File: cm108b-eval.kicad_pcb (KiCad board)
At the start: 2 copper layers, 16 x 35 mm, 3 parts, among them IC1 CM108B, J1 USB_A

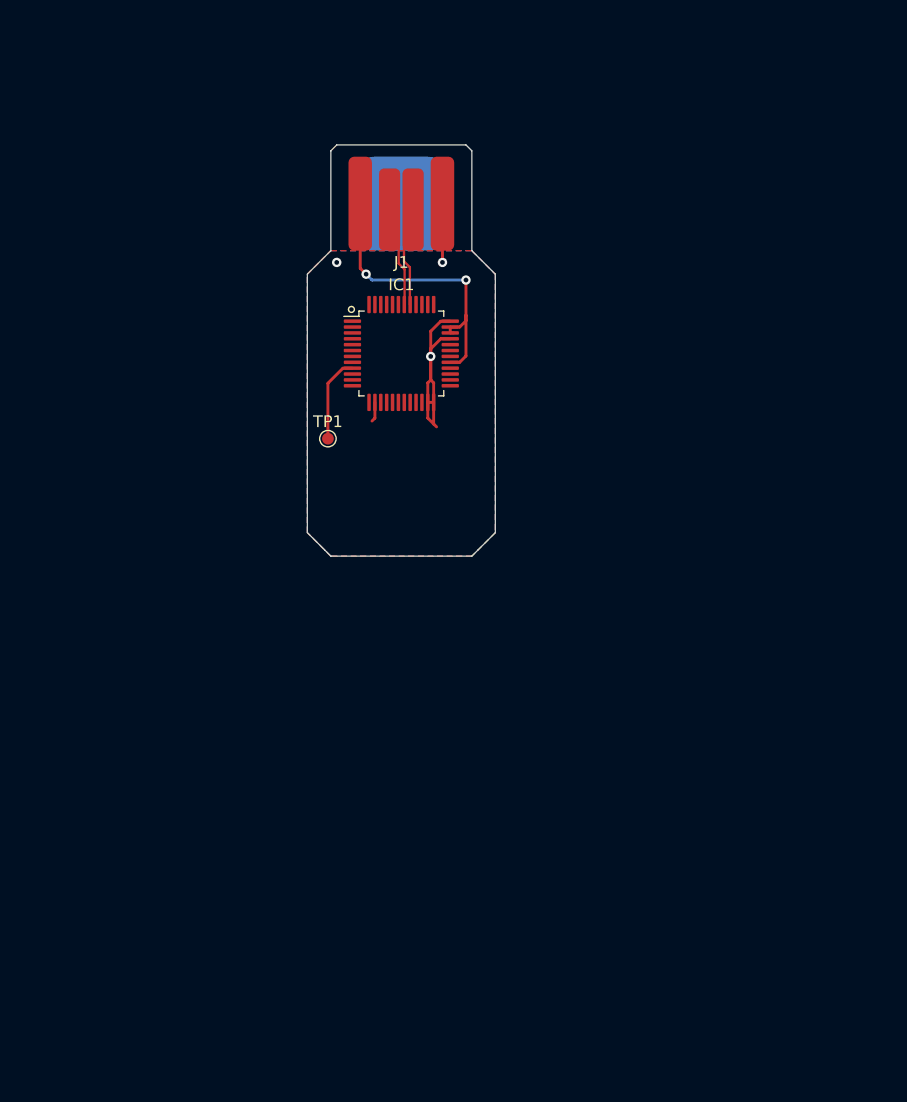
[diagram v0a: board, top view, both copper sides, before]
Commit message: Footprints assigned
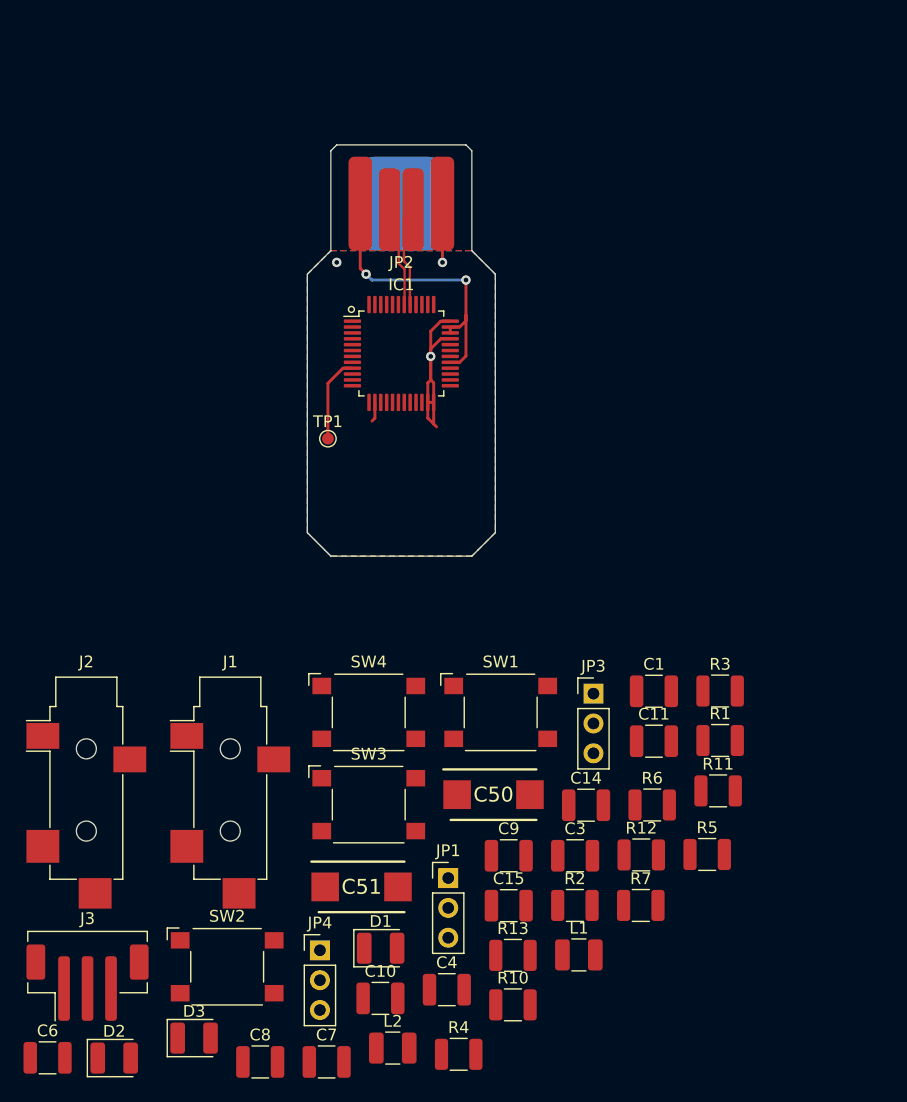
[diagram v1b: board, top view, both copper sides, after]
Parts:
- added C1: 10uF, Capacitor_SMD:C_1210_3225Metric, F.Cu at (170.5, 126.5)
- added C10: 104, Capacitor_SMD:C_1210_3225Metric, F.Cu at (147.2, 152.6)
- added C11: 105, Capacitor_SMD:C_1210_3225Metric, F.Cu at (170.5, 130.8)
- added C14: 475, Capacitor_SMD:C_1210_3225Metric, F.Cu at (164.7, 136.2)
- added C15: 475, Capacitor_SMD:C_1210_3225Metric, F.Cu at (158.1, 144.8)
- added C3: 101, Capacitor_SMD:C_1210_3225Metric, F.Cu at (163.8, 140.5)
- added C4: 101, Capacitor_SMD:C_1210_3225Metric, F.Cu at (152.9, 151.9)
- added C50: 470uF, 293D477X9010E2TE3:CAPPM7343X430N, F.Cu at (156.8, 135.3)
- added C51: 470uF, 293D477X9010E2TE3:CAPPM7343X430N, F.Cu at (145.6, 143.2)
- added C6: 104, Capacitor_SMD:C_1210_3225Metric, F.Cu at (118.9, 157.7)
- added C7: 475, Capacitor_SMD:C_1210_3225Metric, F.Cu at (142.6, 158.1)
- added C8: 104, Capacitor_SMD:C_1210_3225Metric, F.Cu at (137.0, 158.1)
- added C9: 475, Capacitor_SMD:C_1210_3225Metric, F.Cu at (158.1, 140.5)
- added D1: OPER, LED_SMD:LED_1210_3225Metric, F.Cu at (147.2, 148.4)
- added D2: REC_MUTE, LED_SMD:LED_1210_3225Metric, F.Cu at (124.6, 157.7)
- added D3: POWER_DOWN, LED_SMD:LED_1210_3225Metric, F.Cu at (131.4, 156.0)
- added J1: SPRK, Connector_Audio:Jack_3.5mm_CUI_SJ-3524-SMT_Horizontal, F.Cu at (134.4, 133.9)
- added J2: MIC, Connector_Audio:Jack_3.5mm_CUI_SJ-3524-SMT_Horizontal, F.Cu at (122.2, 133.9)
- added J3: RADIO_DATA, Connector_JST:JST_PH_B3B-PH-SM4-TB_1x03-1MP_P2.00mm_Vertical, F.Cu at (122.3, 151.3)
- added JP1: PWRSEL, Connector_PinHeader_2.54mm:PinHeader_1x03_P2.54mm_Vertical, F.Cu at (153.0, 142.4)
- added JP3: MODE, Connector_PinHeader_2.54mm:PinHeader_1x03_P2.54mm_Vertical, F.Cu at (165.3, 126.7)
- added JP4: MSEL, Connector_PinHeader_2.54mm:PinHeader_1x03_P2.54mm_Vertical, F.Cu at (142.1, 148.6)
- added L1: L, Inductor_SMD:L_1210_3225Metric, F.Cu at (164.1, 148.9)
- added L2: L, Inductor_SMD:L_1210_3225Metric, F.Cu at (148.3, 156.9)
- added R1: 22Ω, Resistor_SMD:R_1210_3225Metric, F.Cu at (176.1, 130.7)
- added R10: 2.2kΩ, Resistor_SMD:R_1210_3225Metric, F.Cu at (158.5, 153.2)
- added R11: 330, Resistor_SMD:R_1210_3225Metric, F.Cu at (176.0, 135.0)
- added R12: 330, Resistor_SMD:R_1210_3225Metric, F.Cu at (169.4, 140.4)
- added R13: 1.2kΩ, Resistor_SMD:R_1210_3225Metric, F.Cu at (158.5, 149.0)
- added R2: 22Ω, Resistor_SMD:R_1210_3225Metric, F.Cu at (163.8, 144.7)
- added R3: 0Ω, Resistor_SMD:R_1210_3225Metric, F.Cu at (176.1, 126.5)
- added R4: 0Ω, Resistor_SMD:R_1210_3225Metric, F.Cu at (153.9, 157.4)
- added R5: 0Ω, Resistor_SMD:R_1210_3225Metric, F.Cu at (175.0, 140.4)
- added R6: 0Ω, Resistor_SMD:R_1210_3225Metric, F.Cu at (170.3, 136.2)
- added R7: 330, Resistor_SMD:R_1210_3225Metric, F.Cu at (169.4, 144.7)
- added SW1: MUTE_REC, Button_Switch_SMD:SW_SPST_Omron_B3FS-100xP, F.Cu at (157.5, 128.3)
- added SW2: MUTE_PLAY, Button_Switch_SMD:SW_SPST_Omron_B3FS-100xP, F.Cu at (134.2, 149.9)
- added SW3: VOL_DN, Button_Switch_SMD:SW_SPST_Omron_B3FS-100xP, F.Cu at (146.2, 136.2)
- added SW4: VOL_UP, Button_Switch_SMD:SW_SPST_Omron_B3FS-100xP, F.Cu at (146.2, 128.3)
- renumbered J1 to JP2
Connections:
- IC1 pad 10: (no net) -> /MODE
- IC1 pad 12: (no net) -> /LEDO
- IC1 pad 16: (no net) -> GND
- IC1 pad 18: (no net) -> /MUTEP
- IC1 pad 21: (no net) -> /LEDR
- IC1 pad 22: (no net) -> GND
- IC1 pad 25: (no net) -> Net-(IC1-Pad25)
- IC1 pad 26: (no net) -> Net-(C14-Pad2)
- IC1 pad 27: (no net) -> Net-(C11-Pad2)
- IC1 pad 29: VBUS -> Net-(C6-Pad1)
- IC1 pad 30: (no net) -> Net-(C51-Pad1)
- IC1 pad 32: (no net) -> Net-(C50-Pad1)
- IC1 pad 34: VBUS -> Net-(C8-Pad1)
- IC1 pad 38: (no net) -> /MSEL
- IC1 pad 39: (no net) -> /VOLUP
- IC1 pad 40: (no net) -> /PDSW
- IC1 pad 48: (no net) -> /VOLDN
- IC1 pad 6: (no net) -> /MUTER
- IC1 pad 7: (no net) -> /PWRSEL
- JP2 pad 1: VBUS -> Net-(JP2-Pad1)
- JP2 pad 2: /D- -> Net-(C3-Pad1)
- JP2 pad 3: /D+ -> Net-(C4-Pad1)
- JP2 pad 4: GND -> Net-(JP2-Pad4)
- JP2 pad 5: (no net) -> GND
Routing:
- net Net-(JP2-Pad4): track 0.00 -> 5.00 mm, vias 0 -> 1
- net GND: track 26.3 -> 21.3 mm, vias 3 -> 2

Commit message: PCB laid out
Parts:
- C11: value 105 -> 1uF
- C14, C15, C7, C9: value 475 -> 4.7uF
- C3, C4: value 101 -> 100pF
- C6, C8: value 104 -> 100nF
- D3: value POWER_DOWN -> PWR_DN
- JP2: footprint usb-a-edge:USB-A_trace -> Connector_USB:USB_Micro-B_Molex_47346-0001
- moved L2 82.9 mm to (150.0, 74.0), turned to 180 degrees
- moved SW2 81.3 mm to (183.0, 85.0)
- moved C6 78.7 mm to (169.0, 97.0), turned to 270 degrees
- moved C8 75.2 mm to (169.0, 90.0), turned to 90 degrees
- moved L1 75.2 mm to (170.0, 74.0)
- moved JP4 74.6 mm to (144.0, 74.0)
- moved C10 74.4 mm to (173.5, 83.0), turned to 180 degrees
- moved JP1 71.0 mm to (134.0, 74.0)
- moved C4 70.9 mm to (154.0, 81.0), turned to 270 degrees
- moved C7 68.2 mm to (173.0, 97.0), turned to 270 degrees
- moved R4 66.7 mm to (177.5, 95.0)
- moved R2 64.0 mm to (158.0, 81.0), turned to 90 degrees
- moved J3 62.4 mm to (135.8, 90.4), turned to 90 degrees
- moved C3 59.6 mm to (167.0, 81.0), turned to 270 degrees
- moved SW1 59.1 mm to (183.0, 75.0)
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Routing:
- net /VOLDN: track 0.00 -> 64.6 mm, vias 0 -> 2
- net +3V3: track 7.34 -> 70.2 mm, vias 0 -> 2
- net /AUDIO_R: track 0.00 -> 40.6 mm, vias 0 -> 2
- net /MUTER: track 0.00 -> 36.6 mm, vias 0 -> 2
- net /VOLUP: track 0.00 -> 34.8 mm, vias 0 -> 4
- net /MIC_IN: track 0.00 -> 34.6 mm, vias 0 -> 2
- net /AUDIO_L: track 0.00 -> 32.8 mm
- net /PWRSEL: track 0.00 -> 30.8 mm, vias 0 -> 2
- net /MUTEP: track 0.00 -> 30.1 mm, vias 0 -> 2
- net /PDSW: track 0.00 -> 29.9 mm, vias 0 -> 2
- net /MODE: track 0.00 -> 29.8 mm
- net Net-(C14-Pad2): track 0.00 -> 25.0 mm
- net /MSEL: track 0.00 -> 24.3 mm
- net /MIC_BIAS: track 0.00 -> 23.0 mm
- net Net-(C15-Pad2): track 0.00 -> 19.9 mm
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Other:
- board size 16 x 35 mm -> 60 x 50 mm
- board text added: "CM108B Audio Evaluation Board v1 C. Keller 2021-03-22"
- board text added: "CM108B USB Audio"

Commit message: Completed BOM
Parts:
- C1: value 10uF -> 10μF
- C10: value 104 -> 100nF
- C11: value 1uF -> 1μF
- C14, C15, C7, C9: value 4.7uF -> 4.7μF
- C50, C51: value 470uF -> 470μF
- D1, D2, D3: footprint LED_SMD:LED_1210_3225Metric -> LED_SMD:LED_0603_1608Metric
- J1: value SPRK -> SPKR
- R11, R12, R7: value 330 -> 330Ω
- moved TP1 0.50 mm to (142.5, 117.5)
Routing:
- net Net-(D3-Pad2): track 3.54 -> 4.65 mm
- net Net-(D2-Pad2): track 3.54 -> 4.15 mm
- net Net-(D1-Pad2): track 3.54 -> 4.15 mm
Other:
- board text added: "+"
- board text added: "CM108B Audio Evaluation Board v2 C. Keller 2021-03-23"
- board text removed: "CM108B Audio Evaluation Board v1 C. Keller 2021-03-22"

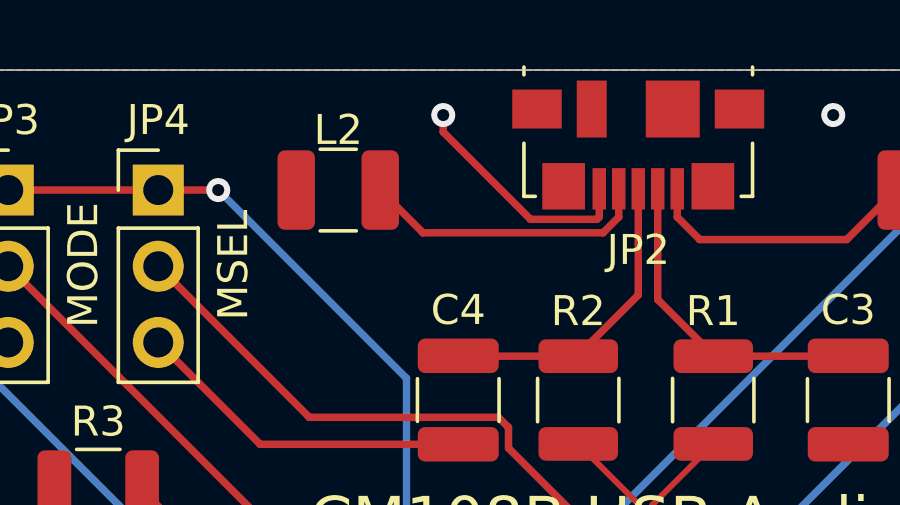
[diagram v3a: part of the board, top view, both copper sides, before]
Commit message: Move inductor to USB cable shield
Having it on the cable's ground pin just doesn't make sense to me.
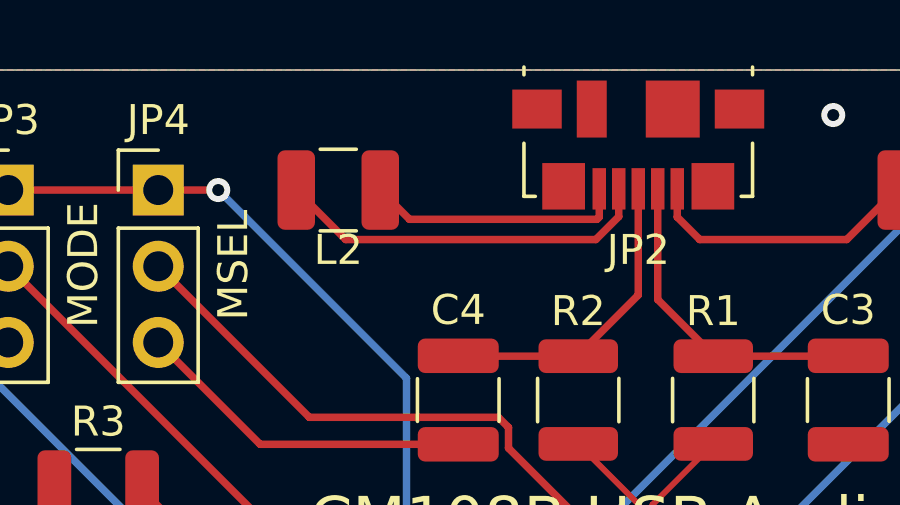
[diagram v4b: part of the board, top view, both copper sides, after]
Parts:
- turned L2 to 0 degrees
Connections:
- JP2 pad 4: Net-(JP2-Pad4) -> GND
- JP2 pad 5: GND -> Net-(JP2-Pad5)
- L2 pad 1: Net-(JP2-Pad4) -> GND
- L2 pad 2: GND -> Net-(JP2-Pad5)
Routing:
- net Net-(JP2-Pad4): track 9.70 -> 0.00 mm
- net Net-(JP2-Pad5): track 0.00 -> 8.67 mm
- net GND: track 41.1 -> 45.9 mm, vias 17 -> 16

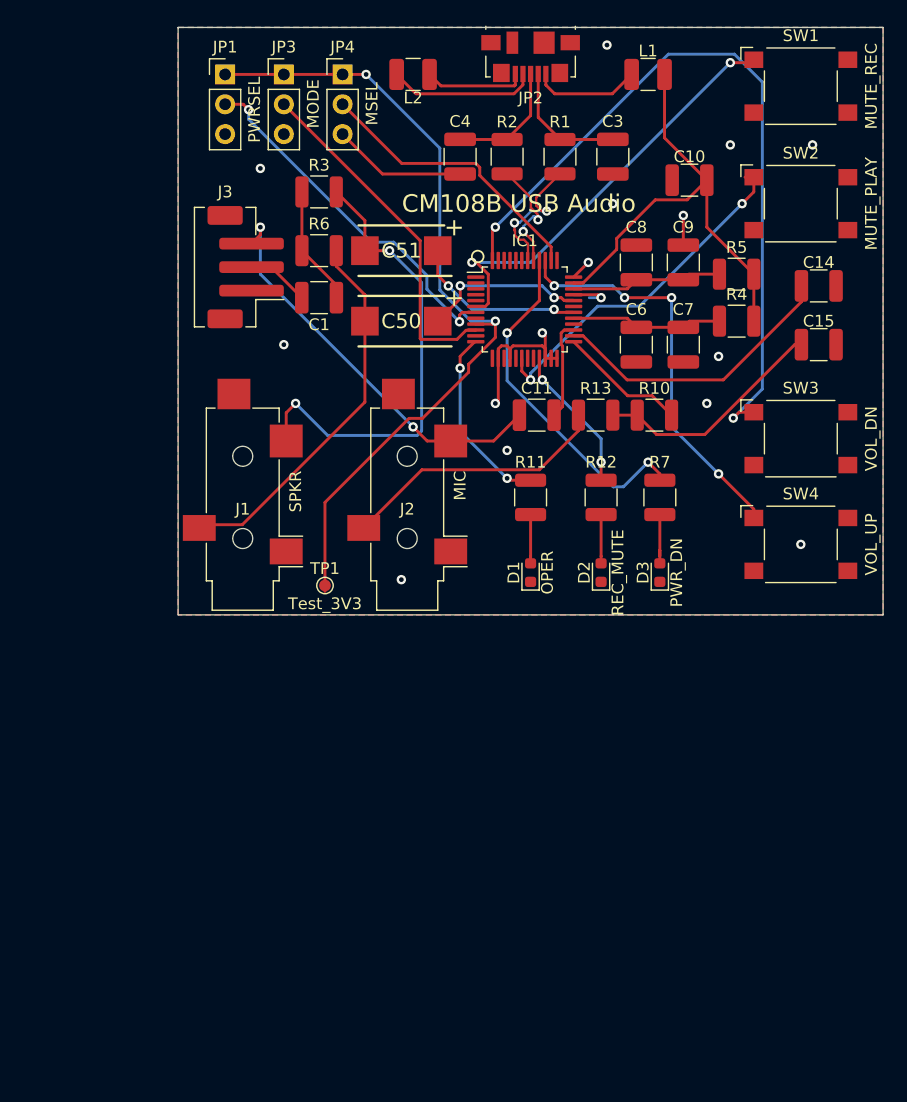
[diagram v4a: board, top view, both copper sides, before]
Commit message: Add some 3D models
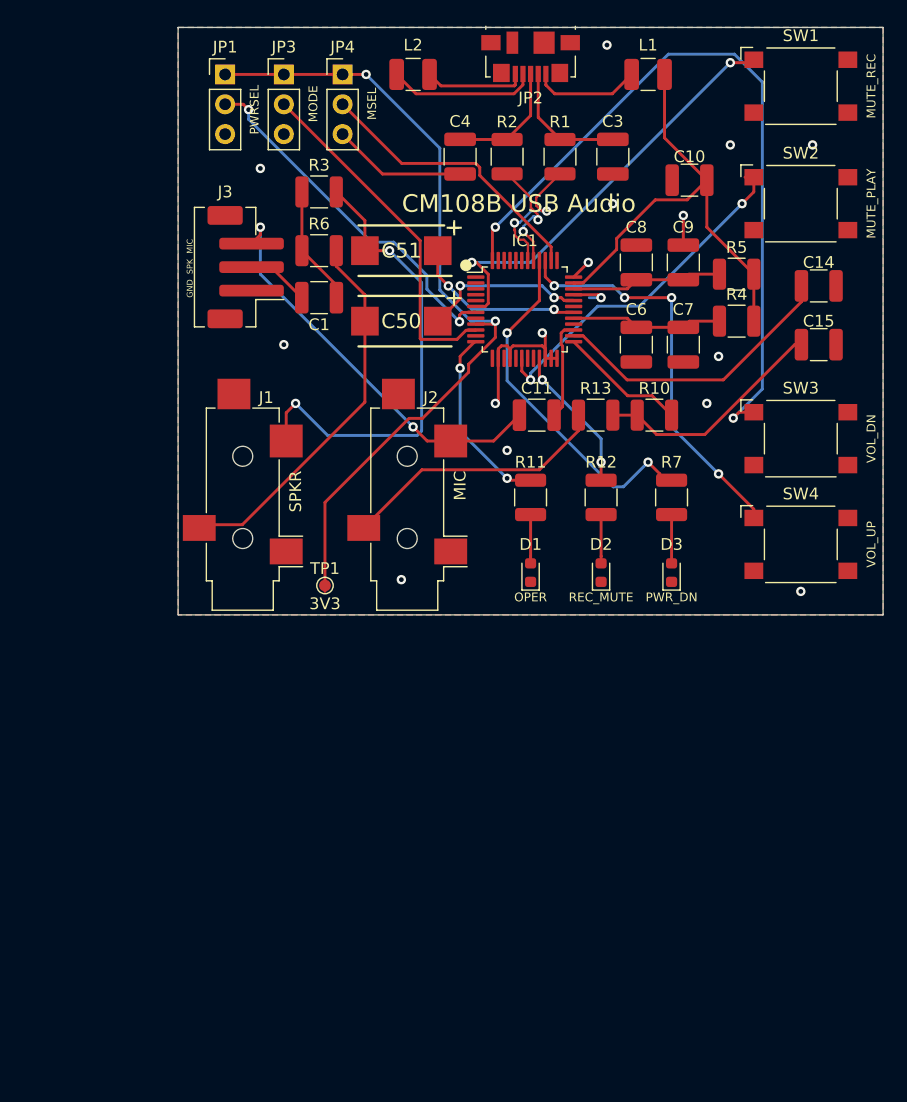
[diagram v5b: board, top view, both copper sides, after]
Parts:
- TP1: value Test_3V3 -> 3V3
- moved D3 1.00 mm to (172.0, 116.4)
- moved R7 1.00 mm to (172.0, 110.0)
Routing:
- net Net-(D3-Pad2): track 4.65 -> 4.15 mm
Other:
- board text added: "CM108B Audio Evaluation Board v3 C. Keller 2021-04-02"
- board text added: "GND SPK MIC"
- board text removed: "CM108B Audio Evaluation Board v2 C. Keller 2021-03-23"

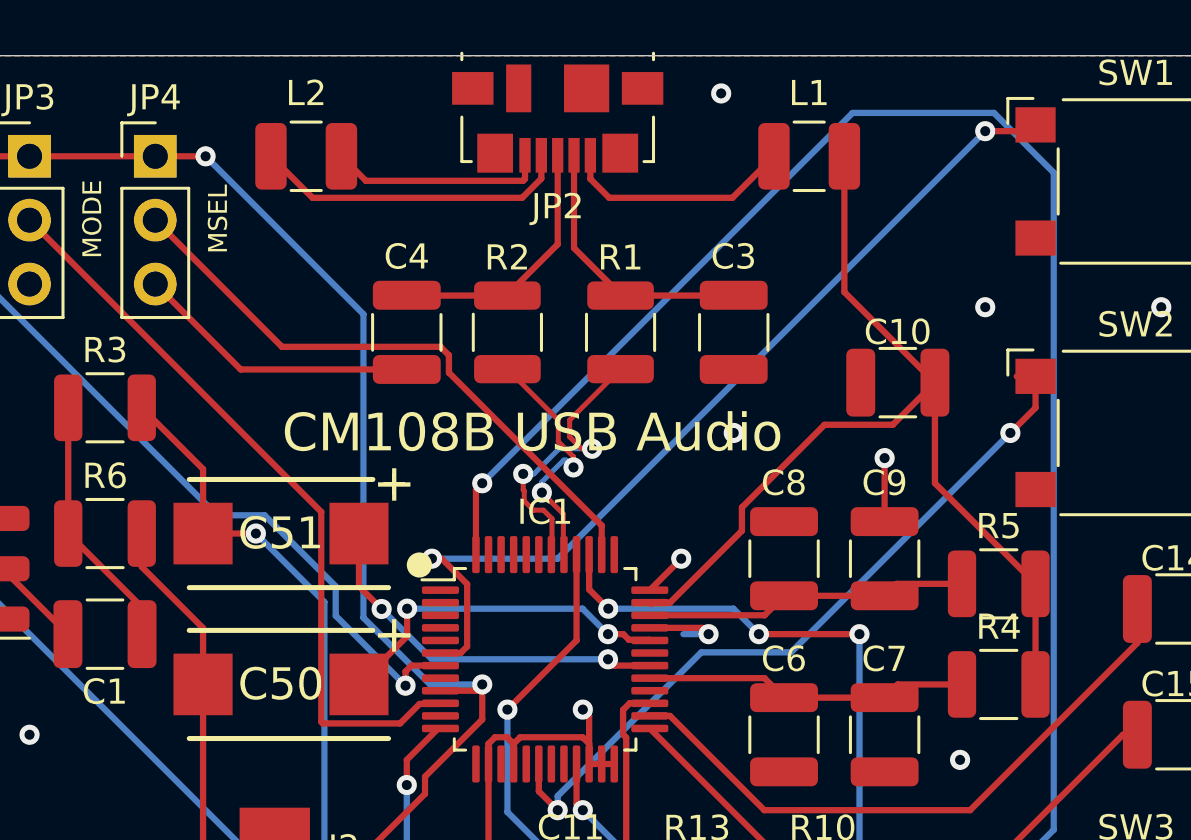
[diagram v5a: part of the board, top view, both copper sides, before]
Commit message: Thicker power traces
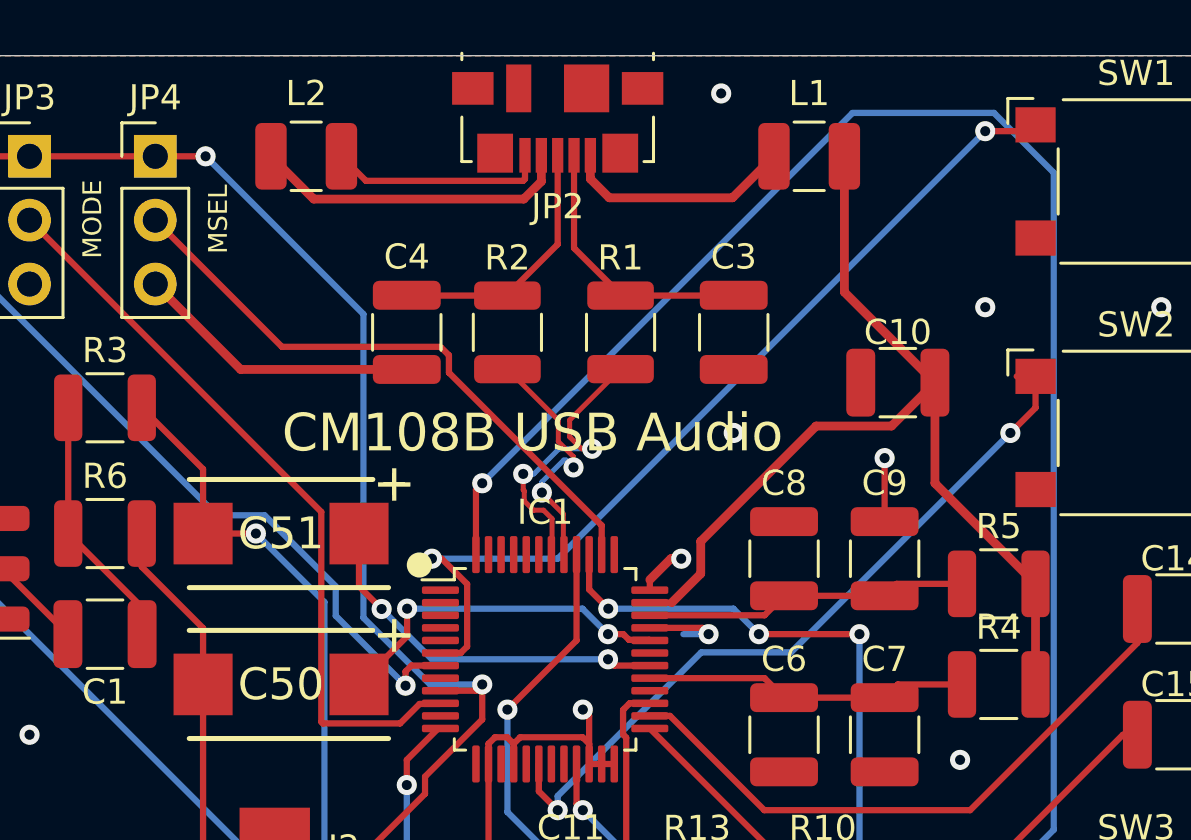
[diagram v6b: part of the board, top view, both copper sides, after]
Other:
- net class Power added: clearance 0.2, trace_width 0.35, via_dia 0.8, via_drill 0.4
- board text added: "CM108B Audio Evaluation Board v3 C. Keller 2021-04-05"
- board text removed: "CM108B Audio Evaluation Board v3 C. Keller 2021-04-02"
